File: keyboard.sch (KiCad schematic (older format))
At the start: 30 parts, among them IC1 ATMEGA32U4, J1 USB C, X1 ASX3F

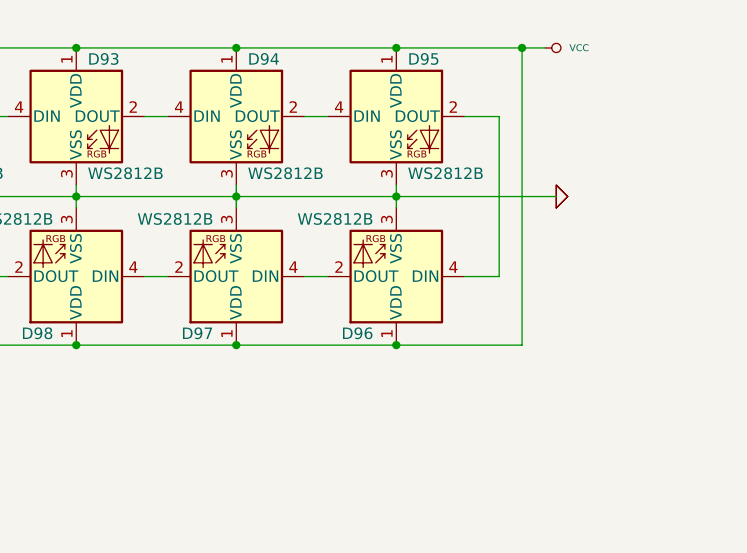
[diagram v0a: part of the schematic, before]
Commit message: Add an additional led to PCB
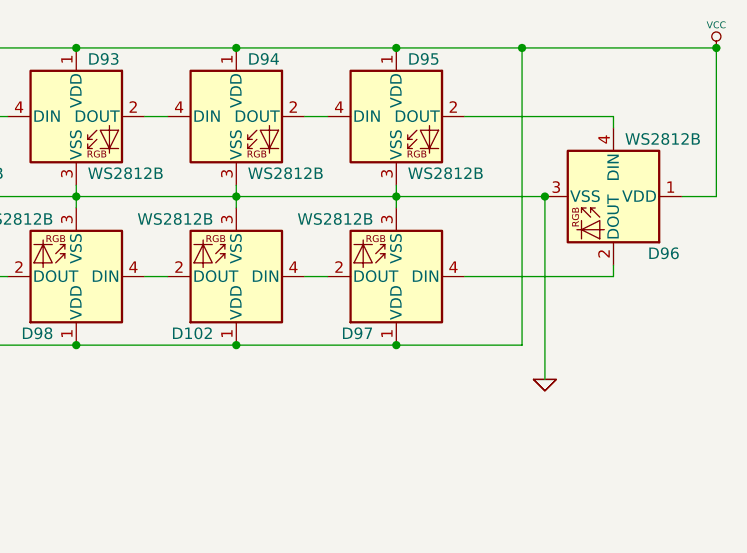
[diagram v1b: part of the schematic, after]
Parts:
- added D102: WS2812B, LED_SMD:LED_WS2812B_PLCC4_5.0x5.0mm_P3.2mm, symbol LED:WS2812B
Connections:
- net GND: now also D102.3 (VSS)
- net VCC: now also D102.1 (VDD)
- net at D97.2 (DOUT): now also D102.4 (DIN); no longer D98.4 (DIN)
- new net: D102.2 (DOUT), D98.4 (DIN)
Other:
- moved on the sheet: D96, D97
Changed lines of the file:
@@
 L LED:WS2812B D96
 U 1 1 61EEB375
+P 10550 1300
+F 0 "D96" V 10800 1450 50  0000 L CNN
+F 1 "WS2812B" V 10300 1350 50  0000 L CNN
+F 2 "LED_SMD:LED_WS2812B_PLCC4_5.0x5.0mm_P3.2mm" H 10600 1000 50  0001 L TNN
+F 3 "https://cdn-shop.adafruit.com/datasheets/WS2812B.pdf" H 10650 925 50  0001 L TNN
+	1    10550 1300
+	0    1    1    0
+$EndComp
+$Comp
+L LED:WS2812B D97
+U 1 1 61EF4C2A
 P 9600 1650
-F 0 "D96" H 9700 1900 50  0000 L CNN
+F 0 "D97" H 9700 1900 50  0000 L CNN
 F 1 "WS2812B" H 9700 1400 50  0000 L CNN
 F 2 "LED_SMD:LED_WS2812B_PLCC4_5.0x5.0mm_P3.2mm" H 9650 1350 50  0001 L TNN
 F 3 "https://cdn-shop.adafruit.com/datasheets/WS2812B.pdf" H 9700 1275 50  0001 L TNN
 	1    9600 1650
-	-1   0    0    1
-$EndComp
-$Comp
-L LED:WS2812B D97
-U 1 1 61EF4C2A
-P 8900 1650
-F 0 "D97" H 9000 1900 50  0000 L CNN
-F 1 "WS2812B" H 9000 1400 50  0000 L CNN
-F 2 "LED_SMD:LED_WS2812B_PLCC4_5.0x5.0mm_P3.2mm" H 8950 1350 50  0001 L TNN
-F 3 "https://cdn-shop.adafruit.com/datasheets/WS2812B.pdf" H 9000 1275 50  0001 L TNN
-	1    8900 1650
 	-1   0    0    1
 $EndComp
@@
 	9200 950  9300 950
 Wire Wire Line
-	9900 950  10050 950
-Wire Wire Line
-	10050 950  10050 1650
-Wire Wire Line
-	10050 1650 9900 1650
-Wire Wire Line
 	9300 1650 9200 1650
 Wire Wire Line
@@
 	8900 650  9600 650
 Connection ~ 8900 650
-Wire Wire Line
-	9600 650  10150 650
 Connection ~ 9600 650
 $Comp
-L power1:VCC #PWR?
+L power1:VCC #PWR0104
 U 1 1 61F82440
-P 10250 650
-F 0 "#PWR?" H 10250 750 30  0001 C CNN
-F 1 "VCC" V 10250 800 30  0000 C CNN
-F 2 "" H 10250 650 60  0001 C CNN
-F 3 "" H 10250 650 60  0001 C CNN
-	1    10250 650
-	0    1    1    0
+P 11000 650
+F 0 "#PWR0104" H 11000 750 30  0001 C CNN
+F 1 "VCC" H 11000 750 30  0000 C CNN
+F 2 "" H 11000 650 60  0001 C CNN
+F 3 "" H 11000 650 60  0001 C CNN
+	1    11000 650
+	1    0    0    -1
 $EndComp
 Wire Wire Line
@@
 Wire Wire Line
 	6100 1300 6100 1350
-$Comp
-L power1:GND #PWR?
-U 1 1 61F952D3
-P 10300 1300
-F 0 "#PWR?" H 10300 1300 30  0001 C CNN
-F 1 "GND" H 10300 1230 30  0001 C CNN
-F 2 "" H 10300 1300 60  0001 C CNN
-F 3 "" H 10300 1300 60  0001 C CNN
-	1    10300 1300
-	0    -1   -1   0
-$EndComp
-$Comp
-L power1:GND #PWR?
-U 1 1 61F952D9
-P 10300 1300
-F 0 "#PWR?" H 10300 1300 30  0001 C CNN
-F 1 "GND" H 10300 1230 30  0001 C CNN
-F 2 "" H 10300 1300 60  0001 C CNN
-F 3 "" H 10300 1300 60  0001 C CNN
-	1    10300 1300
-	0    -1   -1   0
-$EndComp
 Wire Wire Line
 	6800 1250 6800 1300
@@
 Connection ~ 9600 1300
 Wire Wire Line
-	9600 1300 10300 1300
-Wire Wire Line
 	9600 1250 9600 1300
 Wire Wire Line
@@
 	7500 1950 8200 1950
 Connection ~ 7500 1950
-Wire Wire Line
-	8200 1950 8900 1950
 Connection ~ 8200 1950
-Wire Wire Line
-	8900 1950 9600 1950
-Connection ~ 8900 1950
-Wire Wire Line
-	9600 1950 10150 1950
-Wire Wire Line
-	10150 1950 10150 650
-Connection ~ 9600 1950
-Connection ~ 10150 650
-Wire Wire Line
-	10150 650  10250 650
 $Comp
 L LED:WS2812B D90
@@
 Wire Wire Line
 	5800 950  5550 950
+$Comp
+L LED:WS2812B D102
+U 1 1 621C4F51
+P 8900 1650
+F 0 "D102" H 9000 1900 50  0000 L CNN
+F 1 "WS2812B" H 9000 1400 50  0000 L CNN
+F 2 "LED_SMD:LED_WS2812B_PLCC4_5.0x5.0mm_P3.2mm" H 8950 1350 50  0001 L TNN
+F 3 "https://cdn-shop.adafruit.com/datasheets/WS2812B.pdf" H 9000 1275 50  0001 L TNN
+	1    8900 1650
+	-1   0    0    1
+$EndComp
+Wire Wire Line
+	10550 950  10550 1000
+Wire Wire Line
+	9900 950  10550 950
+Wire Wire Line
+	10550 1600 10550 1650
+Wire Wire Line
+	9900 1650 10550 1650
+Wire Wire Line
+	9600 650  10150 650
+Wire Wire Line
+	10150 650  10150 1950
+Connection ~ 10150 650
+Wire Wire Line
+	10150 650  11000 650
+Wire Wire Line
+	10850 1300 11000 1300
+Wire Wire Line
+	11000 1300 11000 650
+Connection ~ 11000 650
+Wire Wire Line
+	10250 1300 9600 1300
+Wire Wire Line
+	8200 1950 8900 1950
+Connection ~ 8900 1950
+$Comp
+L power1:GND #PWR0105
+U 1 1 62250686
+P 10250 2100
+F 0 "#PWR0105" H 10250 2100 30  0001 C CNN
+F 1 "GND" H 10250 2030 30  0001 C CNN
+F 2 "" H 10250 2100 60  0001 C CNN
+F 3 "" H 10250 2100 60  0001 C CNN
+	1    10250 2100
+	1    0    0    -1
+$EndComp
+$Comp
+L power1:GND #PWR0106
+U 1 1 6225068C
+P 10250 2100
+F 0 "#PWR0106" H 10250 2100 30  0001 C CNN
+F 1 "GND" H 10250 2030 30  0001 C CNN
+F 2 "" H 10250 2100 60  0001 C CNN
+F 3 "" H 10250 2100 60  0001 C CNN
+	1    10250 2100
+	1    0    0    -1
+$EndComp
+Wire Wire Line
+	10250 1300 10250 2100
+Wire Wire Line
+	8900 1950 9600 1950
+Connection ~ 9600 1950
+Wire Wire Line
+	9600 1950 10150 1950
+Connection ~ 10250 1300
 Wire Bus Line
 	7300 3300 7300 6500

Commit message: Update BOM in schematic and matrix
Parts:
- C1, C2: LCSC (none) -> C1804
- C3: LCSC (none) -> C28323; Product CL21B105KAFNNNE -> CL21B105KBFNNNE
- C4, C5, C6, C7: LCSC (none) -> C1711
- C8: LCSC (none) -> C28323; Product CL21B104KBCNNNC -> CL21B105KBFNNNE
- D100, D101, D102, D90, D91, D92, D93, D94, D95, D96, D97, D98, D99: LCSC (none) -> C2761795
- IC1: LCSC (none) -> C44854
- J1: LCSC (none) -> C2835315
- R1, R2: LCSC (none) -> C17561
- R3, R4: LCSC (none) -> C27834
- R5, R6: LCSC (none) -> C17414
- S0: LCSC (none) -> C221773
- X1: LCSC (none) -> C258942
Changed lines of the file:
@@
 F 2 "Connector_USB:USB_C_Receptacle_Palconn_UTC16-G" H 2000 5750 50  0001 C CNN
 F 3 "https://www.usb.org/sites/default/files/documents/usb_type-c.zip" H 2000 5750 50  0001 C CNN
+F 4 "C2835315" H 1850 5750 50  0001 C CNN "LCSC"
 	1    1850 5750
 	1    0    0    -1
@@
 F 1 "1u" H 1950 1200 50  0000 L CNN
 F 2 "0805:0805C" H 1900 1300 60  0001 C CNN
-F 3 "http://www.tme.eu/pl/Document/7da762c1dbaf553c64ad9c40d3603826/mlcc_samsung.pdf" H 1900 1300 60  0001 C CNN
+F 3 "" H 1900 1300 60  0001 C CNN
 F 4 "Samsung" H 1900 1300 60  0001 C CNN "Vendor"
-F 5 "CL21B104KBCNNNC" H 1900 1300 60  0001 C CNN "Product"
+F 5 "CL21B105KBFNNNE" H 1900 1300 60  0001 C CNN "Product"
 F 6 "TME" H 1900 1300 60  0001 C CNN "Supplier"
 F 7 "CL21B104KBCNNNC" H 1900 1300 60  0001 C CNN "Supplier Symbol"
+F 8 "C28323" H 1900 1300 50  0001 C CNN "LCSC"
 	1    1900 1300
 	1    0    0    -1
@@
 F 6 "TME" H 2350 3200 60  0001 C CNN "Supplier"
 F 7 "TACTB-64K-F" H 2350 3200 60  0001 C CNN "Supplier Symbol"
+F 8 "C221773" H 2350 3200 50  0001 C CNN "LCSC"
 	1    2350 3200
 	0    1    1    0
@@
 F 6 "DigiKey" H 4850 4900 60  0001 C CNN "Supplier"
 F 7 "ATMEGA32U4-AU-ND" H 4850 4900 60  0001 C CNN "Supplier Symbol"
+F 8 "C44854" H 4850 4900 50  0001 C CNN "LCSC"
 	1    4850 4900
 	1    0    0    -1
@@
 F 6 "TME" H 2650 4350 60  0001 C CNN "Supplier"
 F 7 "CL21C220JBANNNC" H 2650 4350 60  0001 C CNN "Supplier Symbol"
+F 8 "C1804" H 2650 4350 50  0001 C CNN "LCSC"
 	1    2650 4350
 	1    0    0    -1
@@
 F 6 "TME" H 2650 4350 60  0001 C CNN "Supplier"
 F 7 "CL21C220JBANNNC" H 2650 4350 60  0001 C CNN "Supplier Symbol"
+F 8 "C1804" H 3550 4350 50  0001 C CNN "LCSC"
 	1    3550 4350
 	1    0    0    -1
@@
 F 6 "TME" H 2200 1300 60  0001 C CNN "Supplier"
 F 7 "CL21B104KBCNNNC" H 2200 1300 60  0001 C CNN "Supplier Symbol"
+F 8 "C1711" H 2200 1300 50  0001 C CNN "LCSC"
 	1    2200 1300
 	1    0    0    -1
@@
 F 6 "TME" H 2200 1300 60  0001 C CNN "Supplier"
 F 7 "CL21B104KBCNNNC" H 2200 1300 60  0001 C CNN "Supplier Symbol"
+F 8 "C1711" H 2500 1300 50  0001 C CNN "LCSC"
 	1    2500 1300
 	1    0    0    -1
@@
 F 6 "TME" H 2200 1300 60  0001 C CNN "Supplier"
 F 7 "CL21B104KBCNNNC" H 2200 1300 60  0001 C CNN "Supplier Symbol"
+F 8 "C1711" H 2800 1300 50  0001 C CNN "LCSC"
 	1    2800 1300
 	1    0    0    -1
@@
 F 6 "TME" H 2200 1300 60  0001 C CNN "Supplier"
 F 7 "CL21B104KBCNNNC" H 2200 1300 60  0001 C CNN "Supplier Symbol"
+F 8 "C1711" H 3100 1300 50  0001 C CNN "LCSC"
 	1    3100 1300
 	1    0    0    -1
@@
 F 6 "TME" H 3050 5750 60  0001 C CNN "Supplier"
 F 7 "CRCW080522R0JNTABC" H 3050 5750 60  0001 C CNN "Supplier Symbol"
+F 8 "C17561" H 3050 5750 50  0001 C CNN "LCSC"
 	1    3050 5750
 	0    1    1    0
@@
 F 6 "TME" H 3050 5750 60  0001 C CNN "Supplier"
 F 7 "CRCW080522R0JNTABC" H 3050 5750 60  0001 C CNN "Supplier Symbol"
+F 8 "C17561" H 3050 5850 50  0001 C CNN "LCSC"
 	1    3050 5850
 	0    1    1    0
@@
 F 1 "1u" H 3500 6850 50  0000 L CNN
 F 2 "0805:0805C" H 3450 6950 60  0001 C CNN
-F 3 "http://www.jm.pl/karty/CCCX7R.pdf" H 3450 6950 60  0001 C CNN
+F 3 "" H 3450 6950 60  0001 C CNN
 F 4 "Samsung" H 3450 6950 60  0001 C CNN "Vendor"
-F 5 "CL21B105KAFNNNE" H 3450 6950 60  0001 C CNN "Product"
+F 5 "CL21B105KBFNNNE" H 3450 6950 60  0001 C CNN "Product"
 F 6 "TME" H 3450 6950 60  0001 C CNN "Supplier"
 F 7 "CL21B105KAFNNNE" H 3450 6950 60  0001 C CNN "Supplier Symbol"
+F 8 "C28323" H 3450 6950 50  0001 C CNN "LCSC"
 	1    3450 6950
 	1    0    0    -1
@@
 F 6 "TME" H 6600 7250 60  0001 C CNN "Supplier"
 F 7 "CRCW080510K0JNTABC" H 6600 7250 60  0001 C CNN "Supplier Symbol"
+F 8 "C17414" H 6600 7250 50  0001 C CNN "LCSC"
 	1    6600 7250
 	1    0    0    -1
@@
 F 6 "TME" H 4000 6150 60  0001 C CNN "Supplier"
 F 7 "CRCW080510K0JNTABC" H 4000 6150 60  0001 C CNN "Supplier Symbol"
+F 8 "C17414" H 3650 1100 50  0001 C CNN "LCSC"
 	1    3650 1100
 	1    0    0    -1
@@
 F 6 "TME" H 3100 4000 60  0001 C CNN "Supplier"
 F 7 "16.00M-SMDXT324" H 3100 4000 60  0001 C CNN "Supplier Symbol"
+F 8 "C258942" H 3100 4000 50  0001 C CNN "LCSC"
 	1    3100 4000
 	1    0    0    -1
@@
 F 6 "TME" H 3050 5350 60  0001 C CNN "Supplier"
 F 7 "CRCW080522R0JNTABC" H 3050 5350 60  0001 C CNN "Supplier Symbol"
+F 8 "C27834" H 3050 5350 50  0001 C CNN "LCSC"
 	1    3050 5350
 	0    1    1    0
@@
 F 6 "TME" H 3050 5350 60  0001 C CNN "Supplier"
 F 7 "CRCW080522R0JNTABC" H 3050 5350 60  0001 C CNN "Supplier Symbol"
+F 8 "C27834" H 3050 5450 50  0001 C CNN "LCSC"
 	1    3050 5450
 	0    1    1    0
@@
 F 2 "LED_SMD:LED_WS2812B_PLCC4_5.0x5.0mm_P3.2mm" H 6850 650 50  0001 L TNN
 F 3 "https://cdn-shop.adafruit.com/datasheets/WS2812B.pdf" H 6900 575 50  0001 L TNN
+F 4 "C2761795" H 6800 950 50  0001 C CNN "LCSC"
 	1    6800 950
 	1    0    0    -1
@@
 F 2 "LED_SMD:LED_WS2812B_PLCC4_5.0x5.0mm_P3.2mm" H 7550 650 50  0001 L TNN
 F 3 "https://cdn-shop.adafruit.com/datasheets/WS2812B.pdf" H 7600 575 50  0001 L TNN
+F 4 "C2761795" H 7500 950 50  0001 C CNN "LCSC"
 	1    7500 950
 	1    0    0    -1
@@
 F 2 "LED_SMD:LED_WS2812B_PLCC4_5.0x5.0mm_P3.2mm" H 8250 650 50  0001 L TNN
 F 3 "https://cdn-shop.adafruit.com/datasheets/WS2812B.pdf" H 8300 575 50  0001 L TNN
+F 4 "C2761795" H 8200 950 50  0001 C CNN "LCSC"
 	1    8200 950
 	1    0    0    -1
@@
 F 2 "LED_SMD:LED_WS2812B_PLCC4_5.0x5.0mm_P3.2mm" H 8950 650 50  0001 L TNN
 F 3 "https://cdn-shop.adafruit.com/datasheets/WS2812B.pdf" H 9000 575 50  0001 L TNN
+F 4 "C2761795" H 8900 950 50  0001 C CNN "LCSC"
 	1    8900 950
 	1    0    0    -1
@@
 F 2 "LED_SMD:LED_WS2812B_PLCC4_5.0x5.0mm_P3.2mm" H 9650 650 50  0001 L TNN
 F 3 "https://cdn-shop.adafruit.com/datasheets/WS2812B.pdf" H 9700 575 50  0001 L TNN
+F 4 "C2761795" H 9600 950 50  0001 C CNN "LCSC"
 	1    9600 950
 	1    0    0    -1
@@
 F 2 "LED_SMD:LED_WS2812B_PLCC4_5.0x5.0mm_P3.2mm" H 10600 1000 50  0001 L TNN
 F 3 "https://cdn-shop.adafruit.com/datasheets/WS2812B.pdf" H 10650 925 50  0001 L TNN
+F 4 "C2761795" H 10550 1300 50  0001 C CNN "LCSC"
 	1    10550 1300
 	0    1    1    0
@@
 F 2 "LED_SMD:LED_WS2812B_PLCC4_5.0x5.0mm_P3.2mm" H 9650 1350 50  0001 L TNN
 F 3 "https://cdn-shop.adafruit.com/datasheets/WS2812B.pdf" H 9700 1275 50  0001 L TNN
+F 4 "C2761795" H 9600 1650 50  0001 C CNN "LCSC"
 	1    9600 1650
 	-1   0    0    1
@@
 F 2 "LED_SMD:LED_WS2812B_PLCC4_5.0x5.0mm_P3.2mm" H 8250 1350 50  0001 L TNN
 F 3 "https://cdn-shop.adafruit.com/datasheets/WS2812B.pdf" H 8300 1275 50  0001 L TNN
+F 4 "C2761795" H 8200 1650 50  0001 C CNN "LCSC"
 	1    8200 1650
 	-1   0    0    1
@@
 F 2 "LED_SMD:LED_WS2812B_PLCC4_5.0x5.0mm_P3.2mm" H 7550 1350 50  0001 L TNN
 F 3 "https://cdn-shop.adafruit.com/datasheets/WS2812B.pdf" H 7600 1275 50  0001 L TNN
+F 4 "C2761795" H 7500 1650 50  0001 C CNN "LCSC"
 	1    7500 1650
 	-1   0    0    1
@@
 F 2 "LED_SMD:LED_WS2812B_PLCC4_5.0x5.0mm_P3.2mm" H 6850 1350 50  0001 L TNN
 F 3 "https://cdn-shop.adafruit.com/datasheets/WS2812B.pdf" H 6900 1275 50  0001 L TNN
+F 4 "C2761795" H 6800 1650 50  0001 C CNN "LCSC"
 	1    6800 1650
 	-1   0    0    1
@@
 F 2 "LED_SMD:LED_WS2812B_PLCC4_5.0x5.0mm_P3.2mm" H 6150 1350 50  0001 L TNN
 F 3 "https://cdn-shop.adafruit.com/datasheets/WS2812B.pdf" H 6200 1275 50  0001 L TNN
+F 4 "C2761795" H 6100 1650 50  0001 C CNN "LCSC"
 	1    6100 1650
 	-1   0    0    1
@@
 F 2 "LED_SMD:LED_WS2812B_PLCC4_5.0x5.0mm_P3.2mm" H 6150 650 50  0001 L TNN
 F 3 "https://cdn-shop.adafruit.com/datasheets/WS2812B.pdf" H 6200 575 50  0001 L TNN
+F 4 "C2761795" H 6100 950 50  0001 C CNN "LCSC"
 	1    6100 950
 	1    0    0    -1
@@
 F 2 "LED_SMD:LED_WS2812B_PLCC4_5.0x5.0mm_P3.2mm" H 8950 1350 50  0001 L TNN
 F 3 "https://cdn-shop.adafruit.com/datasheets/WS2812B.pdf" H 9000 1275 50  0001 L TNN
+F 4 "C2761795" H 8900 1650 50  0001 C CNN "LCSC"
 	1    8900 1650
 	-1   0    0    1

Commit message: Change footprint for MCU
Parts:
- IC1: footprint tqfp:TQFP44 -> Package_DFN_QFN:QFN-44-1EP_7x7mm_P0.5mm_EP5.2x5.2mm
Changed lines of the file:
@@
 F 0 "IC1" H 4050 6730 50  0000 L BNN
 F 1 "ATMEGA32U4" H 5100 3000 50  0000 L BNN
-F 2 "tqfp:TQFP44" H 5350 2925 50  0001 C CNN
+F 2 "Package_DFN_QFN:QFN-44-1EP_7x7mm_P0.5mm_EP5.2x5.2mm" H 5350 2925 50  0001 C CNN
 F 3 "http://www.atmel.com/dyn/resources/prod_documents/doc7766.pdf" H 4850 4900 60  0001 C CNN
 F 4 "Atmel" H 4850 4900 60  0001 C CNN "Vendor"

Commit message: Connect a few tracks to new QFN-44 package
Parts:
- IC1: LCSC C44854 -> C45874
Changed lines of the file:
@@
 F 6 "DigiKey" H 4850 4900 60  0001 C CNN "Supplier"
 F 7 "ATMEGA32U4-AU-ND" H 4850 4900 60  0001 C CNN "Supplier Symbol"
-F 8 "C44854" H 4850 4900 50  0001 C CNN "LCSC"
+F 8 "C45874" H 4850 4900 50  0001 C CNN "LCSC"
 	1    4850 4900
 	1    0    0    -1

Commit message: Fix cable not connected
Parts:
- C3, C8: LCSC C28323 -> C89190
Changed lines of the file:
@@
 F 6 "TME" H 1900 1300 60  0001 C CNN "Supplier"
 F 7 "CL21B104KBCNNNC" H 1900 1300 60  0001 C CNN "Supplier Symbol"
-F 8 "C28323" H 1900 1300 50  0001 C CNN "LCSC"
+F 8 " C89190" H 1900 1300 50  0001 C CNN "LCSC"
 	1    1900 1300
 	1    0    0    -1
@@
 F 6 "TME" H 3450 6950 60  0001 C CNN "Supplier"
 F 7 "CL21B105KAFNNNE" H 3450 6950 60  0001 C CNN "Supplier Symbol"
-F 8 "C28323" H 3450 6950 50  0001 C CNN "LCSC"
+F 8 " C89190" H 3450 6950 50  0001 C CNN "LCSC"
 	1    3450 6950
 	1    0    0    -1
